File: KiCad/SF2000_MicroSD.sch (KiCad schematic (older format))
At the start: 5 parts, among them J8 Micro_SD_Card_Socket, X1 Oscillator_7.0x5.0mm

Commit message: Add two 74LVC8T245PW for clockport level shifting, run INT6 from clockport with its own track to the FPGA via a spare pin in the U4 CBT, more routing
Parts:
- R1: footprint Resistor_SMD:R_0805_2012Metric_Pad1.20x1.40mm_HandSolder -> Resistor_SMD:R_0603_1608Metric_Pad0.98x0.95mm_HandSolder
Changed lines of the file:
@@
 F 0 "R1" V 3450 4450 50  0000 L CNN
 F 1 "33" V 3350 4450 50  0000 L CNN
-F 2 "Resistor_SMD:R_0805_2012Metric_Pad1.20x1.40mm_HandSolder" H 3350 4500 50  0001 C CNN
+F 2 "Resistor_SMD:R_0603_1608Metric_Pad0.98x0.95mm_HandSolder" H 3350 4500 50  0001 C CNN
 F 3 "~" H 3350 4500 50  0001 C CNN
 	1    3350 4500

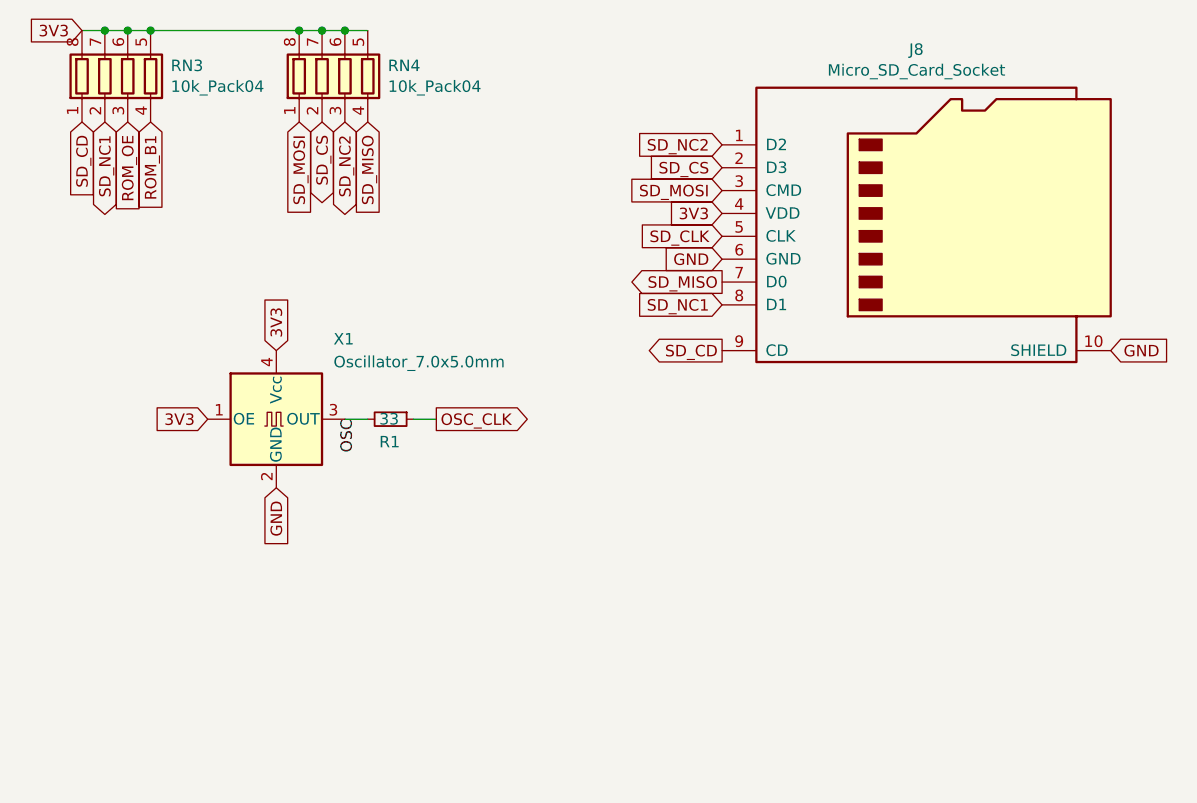
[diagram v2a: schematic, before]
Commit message: Switch to UART1 out from ESP32-C5 module, temporarily route /RTS,/CTS and also EN
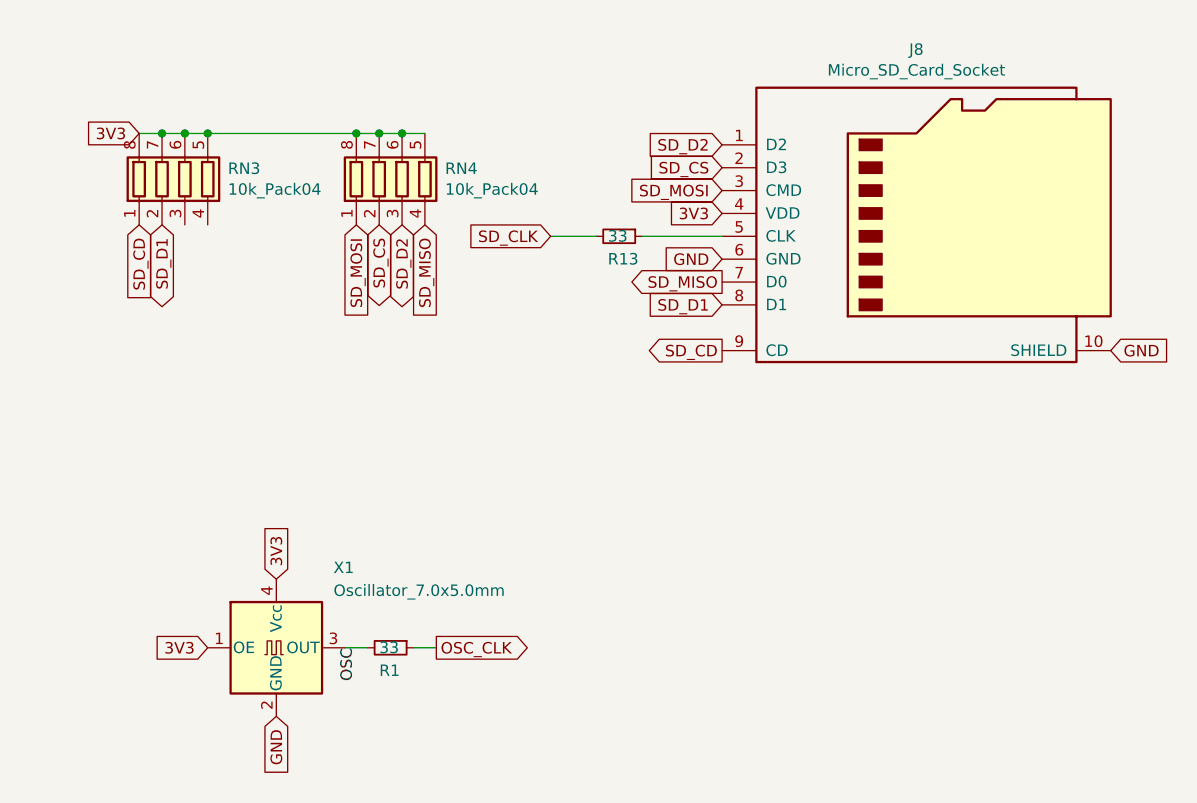
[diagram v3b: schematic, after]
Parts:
- added R13: 33, Resistor_SMD:R_0603_1608Metric_Pad0.98x0.95mm_HandSolder, symbol Device:R_Small
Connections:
- net SD_CLK: now also R13.2; no longer J8.5 (CLK)
- net ROM_B1: no longer names the net of RN3.4 (R4.1)
- net ROM_OE: no longer names the net of RN3.3 (R3.1)
- net SD_NC1 renamed SD_D1
- net SD_NC2 renamed SD_D2
- new net: J8.5 (CLK), R13.1
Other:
- moved on the sheet: R1, RN3, RN4, X1
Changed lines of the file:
@@
 SD_MISO
 Text GLabel 4800 4000 0    50   Input ~ 0
-SD_NC1
+SD_D1
 Text GLabel 4800 3300 0    50   Input ~ 0
-SD_NC2
+SD_D2
 Text GLabel 4800 3400 0    50   Input ~ 0
 SD_CS
@@
 Text GLabel 6500 4200 2    50   Input ~ 0
 GND
-Text GLabel 4800 3700 0    50   Input ~ 0
+Text GLabel 4050 3700 0    50   Input ~ 0
 SD_CLK
 Text GLabel 4800 4200 0    50   Output ~ 0
@@
 L Device:R_Pack04 RN3
 U 1 1 61FDB219
-P 2200 3000
-F 0 "RN3" H 2388 3046 50  0000 L CNN
-F 1 "10k_Pack04" H 2388 2955 50  0000 L CNN
-F 2 "SF2000:RESCAF80P320X160X60-8N" V 2475 3000 50  0001 C CNN
-F 3 "~" H 2200 3000 50  0001 C CNN
-	1    2200 3000
+P 2450 3450
+F 0 "RN3" H 2638 3496 50  0000 L CNN
+F 1 "10k_Pack04" H 2638 3405 50  0000 L CNN
+F 2 "SF2000:RESCAF80P320X160X60-8N" V 2725 3450 50  0001 C CNN
+F 3 "~" H 2450 3450 50  0001 C CNN
+	1    2450 3450
 	1    0    0    -1
 $EndComp
@@
 L Device:R_Pack04 RN4
 U 1 1 61FDC27F
-P 3150 3000
-F 0 "RN4" H 3338 3046 50  0000 L CNN
-F 1 "10k_Pack04" H 3338 2955 50  0000 L CNN
-F 2 "SF2000:RESCAF80P320X160X60-8N" V 3425 3000 50  0001 C CNN
-F 3 "~" H 3150 3000 50  0001 C CNN
-	1    3150 3000
+P 3400 3450
+F 0 "RN4" H 3588 3496 50  0000 L CNN
+F 1 "10k_Pack04" H 3588 3405 50  0000 L CNN
+F 2 "SF2000:RESCAF80P320X160X60-8N" V 3675 3450 50  0001 C CNN
+F 3 "~" H 3400 3450 50  0001 C CNN
+	1    3400 3450
 	1    0    0    -1
 $EndComp
-Text GLabel 2000 2800 0    50   Input ~ 0
+Text GLabel 2250 3250 0    50   Input ~ 0
 3V3
 Wire Wire Line
-	2000 2800 2100 2800
-Connection ~ 2100 2800
+	2250 3250 2350 3250
+Connection ~ 2350 3250
 Wire Wire Line
-	2100 2800 2200 2800
-Connection ~ 2200 2800
+	2350 3250 2450 3250
+Connection ~ 2450 3250
 Wire Wire Line
-	2200 2800 2300 2800
-Connection ~ 2300 2800
+	2450 3250 2550 3250
+Connection ~ 2550 3250
 Wire Wire Line
-	2300 2800 2950 2800
-Connection ~ 2950 2800
+	2550 3250 3200 3250
+Connection ~ 3200 3250
 Wire Wire Line
-	2950 2800 3050 2800
-Connection ~ 3050 2800
+	3200 3250 3300 3250
+Connection ~ 3300 3250
 Wire Wire Line
-	3050 2800 3150 2800
-Connection ~ 3150 2800
+	3300 3250 3400 3250
+Connection ~ 3400 3250
 Wire Wire Line
-	3150 2800 3250 2800
-Text GLabel 3150 3200 3    50   BiDi ~ 0
-SD_NC2
-Text GLabel 3050 3200 3    50   BiDi ~ 0
+	3400 3250 3500 3250
+Text GLabel 3400 3650 3    50   BiDi ~ 0
+SD_D2
+Text GLabel 3300 3650 3    50   BiDi ~ 0
 SD_CS
-Text GLabel 2950 3200 3    50   Input ~ 0
+Text GLabel 3200 3650 3    50   Input ~ 0
 SD_MOSI
-Text GLabel 3250 3200 3    50   Input ~ 0
+Text GLabel 3500 3650 3    50   Input ~ 0
 SD_MISO
-Text GLabel 2100 3200 3    50   BiDi ~ 0
-SD_NC1
-Text GLabel 2000 3200 3    50   Input ~ 0
+Text GLabel 2350 3650 3    50   BiDi ~ 0
+SD_D1
+Text GLabel 2250 3650 3    50   Input ~ 0
 SD_CD
 $Comp
 L Oscillator:SG-8002CA X1
 U 1 1 620EE0AB
-P 2850 4500
-F 0 "X1" H 3100 4850 50  0000 L CNN
-F 1 "Oscillator_7.0x5.0mm" H 3100 4750 50  0000 L CNN
-F 2 "Oscillator:Oscillator_SMD_SeikoEpson_SG8002CA-4Pin_7.0x5.0mm" H 3550 4150 50  0001 C CNN
-F 3 "" H 2750 4500 50  0001 C CNN
-	1    2850 4500
+P 2850 5500
+F 0 "X1" H 3100 5850 50  0000 L CNN
+F 1 "Oscillator_7.0x5.0mm" H 3100 5750 50  0000 L CNN
+F 2 "Oscillator:Oscillator_SMD_SeikoEpson_SG8002CA-4Pin_7.0x5.0mm" H 3550 5150 50  0001 C CNN
+F 3 "" H 2750 5500 50  0001 C CNN
+	1    2850 5500
 	1    0    0    -1
 $EndComp
-Text GLabel 2850 4200 1    50   Input ~ 0
+Text GLabel 2850 5200 1    50   Input ~ 0
 3V3
-Text GLabel 2850 4800 3    50   Input ~ 0
+Text GLabel 2850 5800 3    50   Input ~ 0
 GND
-Text GLabel 3550 4500 2    50   Output ~ 0
+Text GLabel 3550 5500 2    50   Output ~ 0
 OSC_CLK
-Text GLabel 2550 4500 0    50   Input ~ 0
+Text GLabel 2550 5500 0    50   Input ~ 0
 3V3
 $Comp
 L Device:R_Small R?
 U 1 1 68B856DF
-P 3350 4500
+P 3350 5500
 AR Path="/68B856DF" Ref="R?"  Part="1"
 AR Path="/620D263D/68B856DF" Ref="R?"  Part="1"
 AR Path="/62892CF3/68B856DF" Ref="R1"  Part="1"
-F 0 "R1" V 3450 4450 50  0000 L CNN
-F 1 "33" V 3350 4450 50  0000 L CNN
-F 2 "Resistor_SMD:R_0603_1608Metric_Pad0.98x0.95mm_HandSolder" H 3350 4500 50  0001 C CNN
-F 3 "~" H 3350 4500 50  0001 C CNN
-	1    3350 4500
+F 0 "R1" V 3450 5450 50  0000 L CNN
+F 1 "33" V 3350 5450 50  0000 L CNN
+F 2 "Resistor_SMD:R_0603_1608Metric_Pad0.98x0.95mm_HandSolder" H 3350 5500 50  0001 C CNN
+F 3 "~" H 3350 5500 50  0001 C CNN
+	1    3350 5500
 	0    1    1    0
 $EndComp
 Wire Wire Line
-	3550 4500 3450 4500
+	3550 5500 3450 5500
 Wire Wire Line
-	3250 4500 3150 4500
-Text Label 3200 4500 3    50   ~ 0
+	3250 5500 3150 5500
+Text Label 3200 5500 3    50   ~ 0
 OSC
-Text GLabel 2200 3200 3    50   Input ~ 0
-ROM_OE
-Text GLabel 2300 3200 3    50   Input ~ 0
-ROM_B1
+$Comp
+L Device:R_Small R?
+U 1 1 6AFFD5D0
+P 4350 3700
+AR Path="/6AFFD5D0" Ref="R?"  Part="1"
+AR Path="/620D263D/6AFFD5D0" Ref="R?"  Part="1"
+AR Path="/62892CF3/6AFFD5D0" Ref="R13"  Part="1"
+F 0 "R13" V 4450 3650 50  0000 L CNN
+F 1 "33" V 4350 3650 50  0000 L CNN
+F 2 "Resistor_SMD:R_0603_1608Metric_Pad0.98x0.95mm_HandSolder" H 4350 3700 50  0001 C CNN
+F 3 "~" H 4350 3700 50  0001 C CNN
+	1    4350 3700
+	0    1    1    0
+$EndComp
+Wire Wire Line
+	4050 3700 4250 3700
+Wire Wire Line
+	4450 3700 4800 3700
 $EndSCHEMATC

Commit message: Add RP2354A
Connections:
- net CTS: now reaches RN3.4 (R4.1)
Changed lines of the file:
@@
 $Descr A4 11693 8268
 encoding utf-8
-Sheet 5 6
+Sheet 5 7
 Title ""
 Date ""
@@
 Wire Wire Line
 	4450 3700 4800 3700
+Text GLabel 2550 3650 3    50   Input ~ 0
+CTS
 $EndSCHEMATC

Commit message: Add SPI header and rename some signals coming from the ESP32-C5
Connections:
- net CTS renamed ESP32_CTS
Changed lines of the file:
@@
 	4450 3700 4800 3700
 Text GLabel 2550 3650 3    50   Input ~ 0
-CTS
+ESP32_CTS
 $EndSCHEMATC

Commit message: Remove 7x5mm crystal oscillator and add 5x3.2 mm crystal oscillator
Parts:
- removed R1: 33, Resistor_SMD:R_0603_1608Metric_Pad0.98x0.95mm_HandSolder, symbol Device:R_Small
- removed X1: Oscillator_7.0x5.0mm, Oscillator:Oscillator_SMD_SeikoEpson_SG8002CA-4Pin_7.0x5.0mm, symbol Oscillator:SG-8002CA
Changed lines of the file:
@@
 SD_CD
-$Comp
-L Oscillator:SG-8002CA X1
-U 1 1 620EE0AB
-P 2850 5500
-F 0 "X1" H 3100 5850 50  0000 L CNN
-F 1 "Oscillator_7.0x5.0mm" H 3100 5750 50  0000 L CNN
-F 2 "Oscillator:Oscillator_SMD_SeikoEpson_SG8002CA-4Pin_7.0x5.0mm" H 3550 5150 50  0001 C CNN
-F 3 "" H 2750 5500 50  0001 C CNN
-	1    2850 5500
-	1    0    0    -1
-$EndComp
-Text GLabel 2850 5200 1    50   Input ~ 0
-3V3
-Text GLabel 2850 5800 3    50   Input ~ 0
-GND
-Text GLabel 3550 5500 2    50   Output ~ 0
-OSC_CLK
-Text GLabel 2550 5500 0    50   Input ~ 0
-3V3
-$Comp
-L Device:R_Small R?
-U 1 1 68B856DF
-P 3350 5500
-AR Path="/68B856DF" Ref="R?"  Part="1"
-AR Path="/620D263D/68B856DF" Ref="R?"  Part="1"
-AR Path="/62892CF3/68B856DF" Ref="R1"  Part="1"
-F 0 "R1" V 3450 5450 50  0000 L CNN
-F 1 "33" V 3350 5450 50  0000 L CNN
-F 2 "Resistor_SMD:R_0603_1608Metric_Pad0.98x0.95mm_HandSolder" H 3350 5500 50  0001 C CNN
-F 3 "~" H 3350 5500 50  0001 C CNN
-	1    3350 5500
-	0    1    1    0
-$EndComp
-Wire Wire Line
-	3550 5500 3450 5500
-Wire Wire Line
-	3250 5500 3150 5500
-Text Label 3200 5500 3    50   ~ 0
-OSC
 $Comp
 L Device:R_Small R?
